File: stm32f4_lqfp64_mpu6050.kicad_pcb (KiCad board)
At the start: 4 copper layers, 130 x 100 mm, 82 parts, among them M5 ALIS-CUSTOM-PARTS_POWERPADS, P1 CONN_01X08, P2 CONN_02X08, Q5 BSS138, Q6 CRYSTAL_50X32, U1 STM32F405R, U2 MPU6050, U3 LP2985LV, U4 LP2985LV, U5 W25Q80BV, U6 LM1881, U7 TS5A3160, U8 TS5A3160, X1 CON-JST_SM04B-SRSS-TB, X2 CON-JST_SM04B-SRSS-TB, X3 CON-JST_SM04B-SRSS-TB, X4 CON-JST_SM04B-SRSS-TB

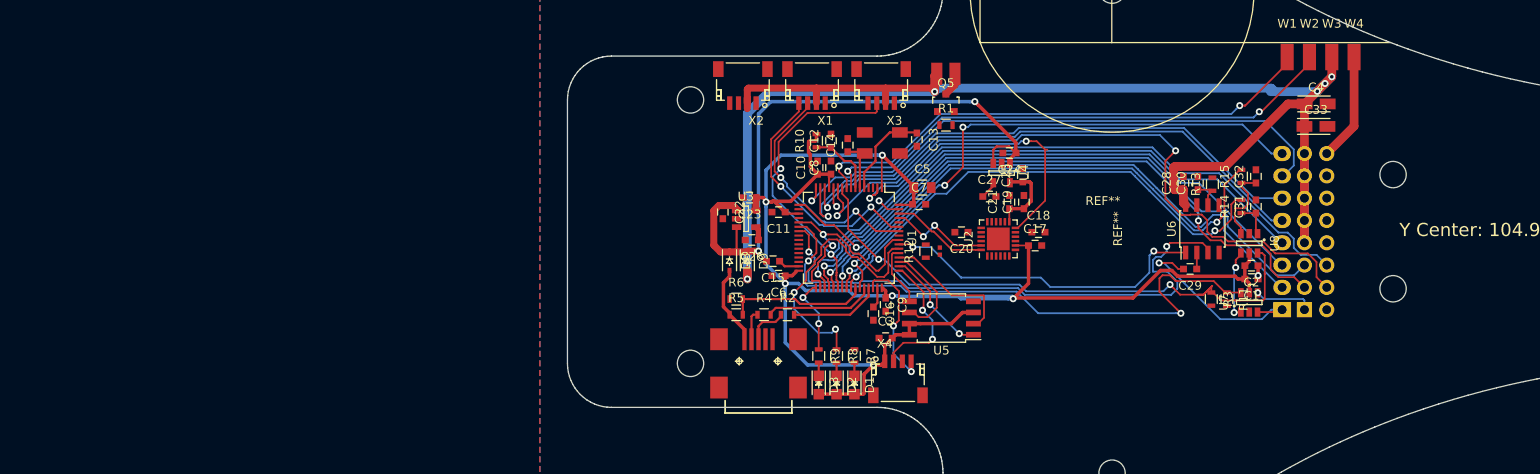
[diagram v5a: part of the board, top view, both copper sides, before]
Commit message: best relative placement
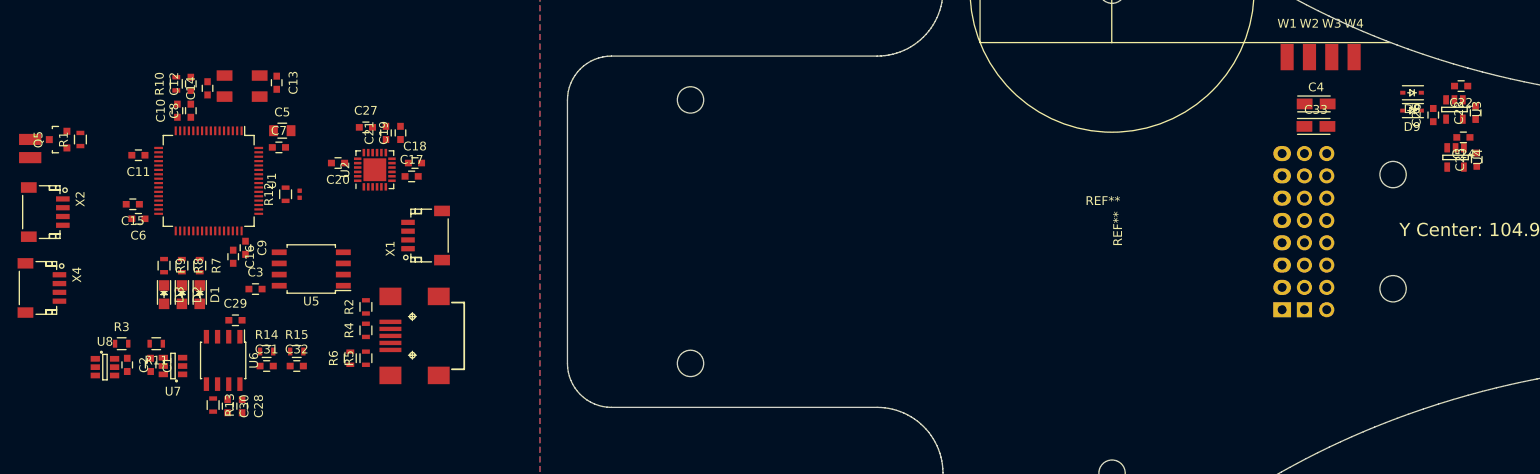
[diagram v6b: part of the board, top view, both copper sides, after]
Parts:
- removed X3: CON-JST_SM04B-SRSS-TB, Connectors_JST_SH:Connectors_JST_SM04B-SRSS-TB
- moved U8 131.1 mm to (30.5, 120.4), turned to 0 degrees
- moved C2 128.5 mm to (33.0, 120.1), turned to 270 degrees
- moved C1 125.7 mm to (35.7, 120.1), turned to 270 degrees
- moved R3 124.2 mm to (32.4, 117.7), turned to 0 degrees
- moved U7 122.8 mm to (38.2, 120.3), turned to 180 degrees
- moved R11 122.0 mm to (36.3, 117.7), turned to 180 degrees
- moved R13 116.5 mm to (42.8, 124.7), turned to 270 degrees
- moved C31 114.1 mm to (48.9, 120.3), turned to 0 degrees
- moved C30 113.4 mm to (44.5, 124.8), turned to 270 degrees
- moved U6 112.5 mm to (43.9, 119.6), turned to 270 degrees
- moved R14 112.2 mm to (48.9, 118.6), turned to 0 degrees
- moved C32 111.3 mm to (52.3, 120.3), turned to 0 degrees
- moved C28 110.2 mm to (46.1, 124.8), turned to 270 degrees
- moved R15 109.4 mm to (52.3, 118.6), turned to 0 degrees
- moved C29 108.9 mm to (45.3, 115.1), turned to 0 degrees
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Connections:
- U1 pad 24: Net-(U1-Pad24) -> MCU_BUZZER
- U1 pad 29: FLEXI_TX/SCL -> FLEXI_TX/SCL2
- U1 pad 30: FLEXI_RX/SDA/DSM -> FLEXI_RX/DSM/SDA2
- X2 pad 3: FLEXI_TX -> FLEXI_TX/SCL2
- X2 pad 4: FLEXI_RX/DSM -> FLEXI_RX/DSM/SDA2
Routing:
- net 3.3V: track 184.0 -> 0.00 mm, vias 6 -> 0
- net VBAT: track 174.8 -> 0.00 mm, vias 5 -> 0
- net TIM8_CH2/FRSKY_RSSI/DSM: track 101.9 -> 0.00 mm, vias 2 -> 0
- net ADC3: track 77.1 -> 0.00 mm, vias 2 -> 0
- net TIM5_CH4: track 71.6 -> 0.00 mm, vias 2 -> 0
- net reg_vin: track 70.1 -> 0.00 mm, vias 2 -> 0
- net TIM8_CH1: track 68.6 -> 0.00 mm, vias 1 -> 0
- net BW_MASK: track 67.8 -> 0.00 mm, vias 2 -> 0
- net TIM12_CH1/PPM: track 66.3 -> 0.00 mm, vias 1 -> 0
- net TIM12_CH2: track 66.0 -> 0.00 mm, vias 1 -> 0
- net BW_LEVEL: track 65.7 -> 0.00 mm, vias 2 -> 0
- net TIM5_CH2: track 65.4 -> 0.00 mm, vias 1 -> 0
- net TIM5_CH3: track 65.3 -> 0.00 mm, vias 1 -> 0
- net TIM8_CH3: track 65.1 -> 0.00 mm, vias 1 -> 0
- net VSYNC_EXTI: track 63.7 -> 0.00 mm, vias 2 -> 0
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
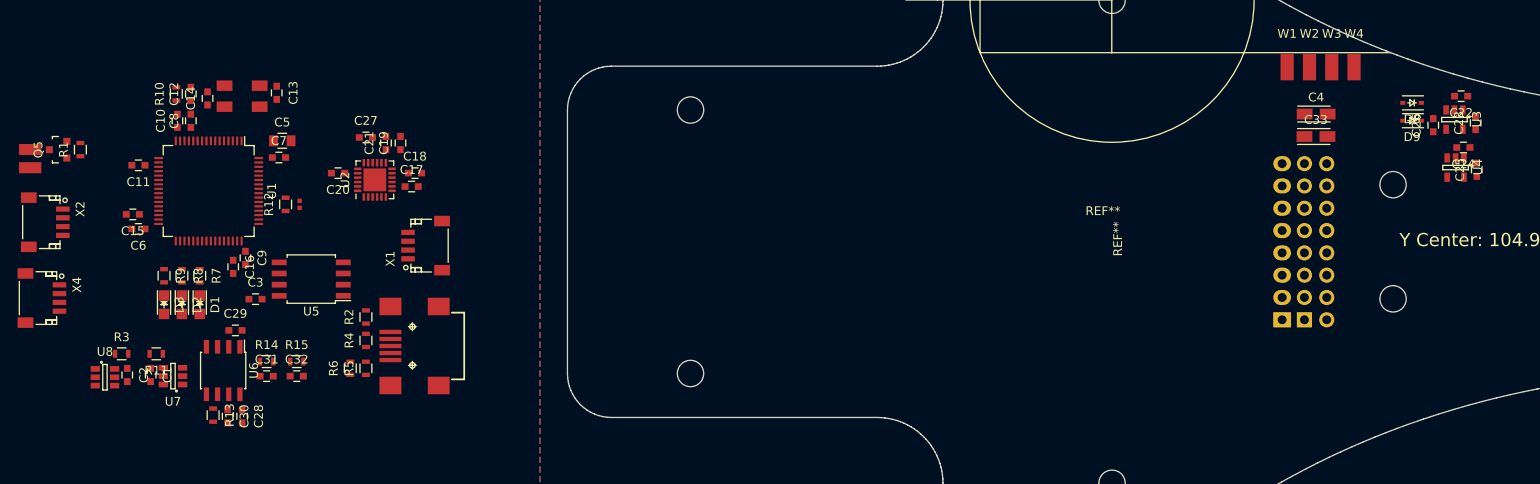
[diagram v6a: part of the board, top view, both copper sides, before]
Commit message: first pass routing complete
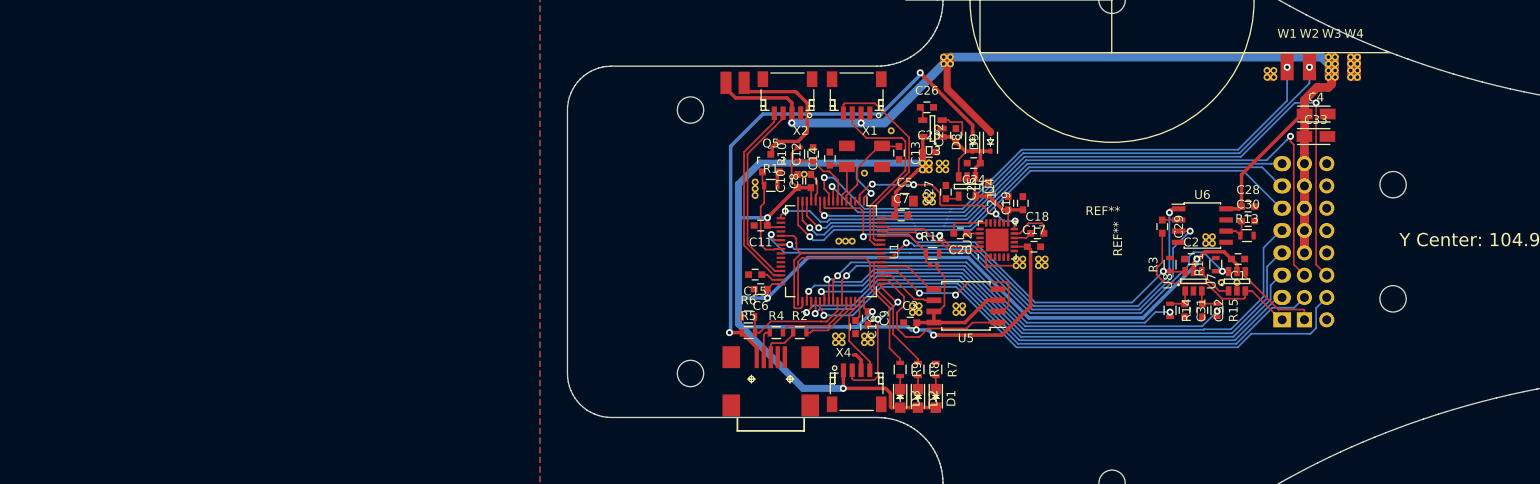
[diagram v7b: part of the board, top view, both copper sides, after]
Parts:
- added ?: , alis_parts:via_04, F.Cu at (114.4, 115.7)
- added ?: , alis_parts:via_04, F.Cu at (162.8, 85.5)
- added ?: , alis_parts:via_04, F.Cu at (163.6, 86.2)
- added ?: , alis_parts:via_04, F.Cu at (162.8, 86.2)
- added ?: , alis_parts:via_04, F.Cu at (124.7, 99.7)
- added ?: , alis_parts:via_04, F.Cu at (124.0, 99.7)
- added ?: , alis_parts:via_04, F.Cu at (124.0, 100.5)
- added ?: , alis_parts:via_04, F.Cu at (125.5, 96.8)
- added ?: , alis_parts:via_04, F.Cu at (126.2, 96.8)
- added ?: , alis_parts:via_04, F.Cu at (126.2, 96.0)
- added ?: , alis_parts:via_04, F.Cu at (125.5, 96.0)
- added ?: , alis_parts:via_04, F.Cu at (113.7, 116.5)
- added ?: , alis_parts:via_04, F.Cu at (124.7, 100.5)
- added ?: , alis_parts:via_04, F.Cu at (135.0, 107.7)
- added ?: , alis_parts:via_04, F.Cu at (135.0, 106.9)
- added ?: , alis_parts:via_04, F.Cu at (134.2, 106.9)
- added ?: , alis_parts:via_04, F.Cu at (134.2, 107.7)
- added ?: , alis_parts:via_04, F.Cu at (157.6, 109.6)
- added ?: , alis_parts:via_04, F.Cu at (159.4, 109.6)
- added ?: , alis_parts:via_04, F.Cu at (156.6, 104.4)
- added ?: , alis_parts:via_04, F.Cu at (156.6, 105.2)
- added ?: , alis_parts:via_04, F.Cu at (155.8, 104.4)
- added ?: , alis_parts:via_04, F.Cu at (113.7, 115.7)
- added ?: , alis_parts:via_04, F.Cu at (155.8, 105.2)
- added ?: , alis_parts:via_04, F.Cu at (136.8, 106.9)
- added ?: , alis_parts:via_04, F.Cu at (137.5, 106.9)
- added ?: , alis_parts:via_04, F.Cu at (137.5, 107.7)
- added ?: , alis_parts:via_04, F.Cu at (136.8, 107.7)
- added ?: , alis_parts:via_04, F.Cu at (123.6, 96.0)
- added ?: , alis_parts:via_04, F.Cu at (127.4, 113.0)
- added ?: , alis_parts:via_04, F.Cu at (128.1, 113.0)
- added ?: , alis_parts:via_04, F.Cu at (128.1, 112.3)
- added ?: , alis_parts:via_04, F.Cu at (127.4, 112.3)
- added ?: , alis_parts:via_04, F.Cu at (114.4, 116.5)
- added ?: , alis_parts:via_04, F.Cu at (117.0, 115.7)
- added ?: , alis_parts:via_04, F.Cu at (117.0, 116.5)
- added ?: , alis_parts:via_04, F.Cu at (117.7, 116.5)
- added ?: , alis_parts:via_04, F.Cu at (117.7, 115.7)
- added ?: , alis_parts:via_04, F.Cu at (123.2, 112.3)
- added ?: , alis_parts:via_04, F.Cu at (122.4, 112.3)
- added ?: , alis_parts:via_04, F.Cu at (122.4, 113.0)
- added ?: , alis_parts:via_04, F.Cu at (123.2, 113.0)
- added ?: , alis_parts:via_04, F.Cu at (104.5, 99.7)
- added ?: , alis_parts:via_04, F.Cu at (104.5, 98.9)
- added ?: , alis_parts:via_04, F.Cu at (114.0, 104.9)
- added ?: , alis_parts:via_04, F.Cu at (104.5, 98.2)
- added ?: , alis_parts:via_04, F.Cu at (123.6, 96.8)
- added ?: , alis_parts:via_04, F.Cu at (124.3, 96.8)
- added ?: , alis_parts:via_04, F.Cu at (124.3, 96.0)
- added ?: , alis_parts:via_04, F.Cu at (169.8, 86.2)
- added ?: , alis_parts:via_04, F.Cu at (169.8, 85.5)
- added ?: , alis_parts:via_04, F.Cu at (170.6, 85.5)
- added ?: , alis_parts:via_04, F.Cu at (170.6, 86.2)
- added ?: , alis_parts:via_04, F.Cu at (169.8, 84.7)
- added ?: , alis_parts:via_04, F.Cu at (169.8, 83.9)
- added ?: , alis_parts:via_04, F.Cu at (114.8, 104.9)
- added ?: , alis_parts:via_04, F.Cu at (170.6, 83.9)
- added ?: , alis_parts:via_04, F.Cu at (170.6, 84.7)
- added ?: , alis_parts:via_04, F.Cu at (126.7, 84.7)
- added ?: , alis_parts:via_04, F.Cu at (126.0, 84.7)
- added ?: , alis_parts:via_04, F.Cu at (126.0, 83.9)
- added ?: , alis_parts:via_04, F.Cu at (126.7, 83.9)
- added ?: , alis_parts:via_04, F.Cu at (172.3, 86.2)
- added ?: , alis_parts:via_04, F.Cu at (173.1, 86.2)
- added ?: , alis_parts:via_04, F.Cu at (172.3, 85.5)
- added ?: , alis_parts:via_04, F.Cu at (173.1, 85.5)
- added ?: , alis_parts:via_04, F.Cu at (115.6, 104.9)
- added ?: , alis_parts:via_04, F.Cu at (172.3, 84.7)
- added ?: , alis_parts:via_04, F.Cu at (173.1, 84.7)
- added ?: , alis_parts:via_04, F.Cu at (173.1, 83.9)
- added ?: , alis_parts:via_04, F.Cu at (117.0, 97.2)
- added ?: , alis_parts:via_04, F.Cu at (172.3, 83.9)
- added ?: , alis_parts:via_04, F.Cu at (120.0, 92.3)
- added ?: , alis_parts:via_04, F.Cu at (110.1, 97.3)
- added ?: , alis_parts:via_04, F.Cu at (163.6, 85.5)
- moved C1 124.5 mm to (159.5, 106.9), turned to 180 degrees
- moved U8 124.4 mm to (154.4, 109.5), turned to 90 degrees
- moved C2 121.9 mm to (154.2, 106.9), turned to 0 degrees
- moved U7 121.6 mm to (159.4, 109.5), turned to 90 degrees
- moved R11 121.1 mm to (157.0, 107.6), turned to 90 degrees
- moved R3 119.8 mm to (151.8, 107.6), turned to 90 degrees
- moved R13 119.5 mm to (160.5, 104.3), turned to 0 degrees
- moved C30 118.3 mm to (160.7, 102.6), turned to 0 degrees
- moved C28 117.0 mm to (160.7, 101.0), turned to 0 degrees
- moved U6 112.7 mm to (155.4, 103.1), turned to 0 degrees
- moved C29 106.2 mm to (150.9, 103.3), turned to 270 degrees
- moved R15 104.9 mm to (157.1, 112.8), turned to 270 degrees
- moved C31 104.8 mm to (153.4, 112.8), turned to 270 degrees
- moved C32 103.4 mm to (155.4, 112.8), turned to 270 degrees
- moved R14 103.0 mm to (151.8, 112.8), turned to 270 degrees
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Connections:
- P1 pad 2: TIM8_CH3 -> TIM12_CH2
- P1 pad 3: TIM12_CH2 -> TIM8_CH3
- P1 pad 5: TIM5_CH1 -> TIM8_CH4
- P1 pad 6: TIM5_CH2 -> TIM5_CH3
- P1 pad 7: TIM5_CH3 -> TIM5_CH2
- P1 pad 8: TIM8_CH4 -> TIM5_CH1
- P2 pad 3: TIM5_CH4 -> TIM8_CH1
- P2 pad 4: ADC3 -> TIM8_CH2/FRSKY_RSSI/DSM
- P2 pad 5: TIM8_CH1 -> TIM5_CH4
- P2 pad 6: TIM8_CH2/FRSKY_RSSI/DSM -> ADC3
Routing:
- net 3.3V: track 0.00 -> 246.9 mm, vias 0 -> 8
- net VBAT: track 0.00 -> 171.9 mm, vias 0 -> 2
- net ADC3: track 0.00 -> 83.3 mm, vias 0 -> 2
- net TIM5_CH4: track 0.00 -> 79.6 mm, vias 0 -> 2
- net TIM8_CH2/FRSKY_RSSI/DSM: track 0.00 -> 66.9 mm, vias 0 -> 1
- net ADC2: track 0.00 -> 66.0 mm, vias 0 -> 2
- net TIM8_CH4: track 0.00 -> 65.9 mm, vias 0 -> 1
- net ADC1: track 0.00 -> 65.2 mm, vias 0 -> 2
- net TIM12_CH1/PPM: track 0.00 -> 64.7 mm, vias 0 -> 1
- net TIM5_CH3: track 0.00 -> 63.6 mm, vias 0 -> 1
- net TIM8_CH1: track 0.00 -> 63.6 mm, vias 0 -> 1
- net BW_MASK: track 0.00 -> 63.4 mm, vias 0 -> 2
- net TIM12_CH2: track 0.00 -> 62.1 mm, vias 0 -> 1
- net TIM5_CH2: track 0.00 -> 61.5 mm, vias 0 -> 1
- net TIM8_CH3: track 0.00 -> 61.1 mm, vias 0 -> 1
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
